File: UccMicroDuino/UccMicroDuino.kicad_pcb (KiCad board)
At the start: 2 copper layers, 45 x 53.5 mm, 14 parts, among them J1 Header, J2 USB_PCB_A, U1 ATtiny85-20S

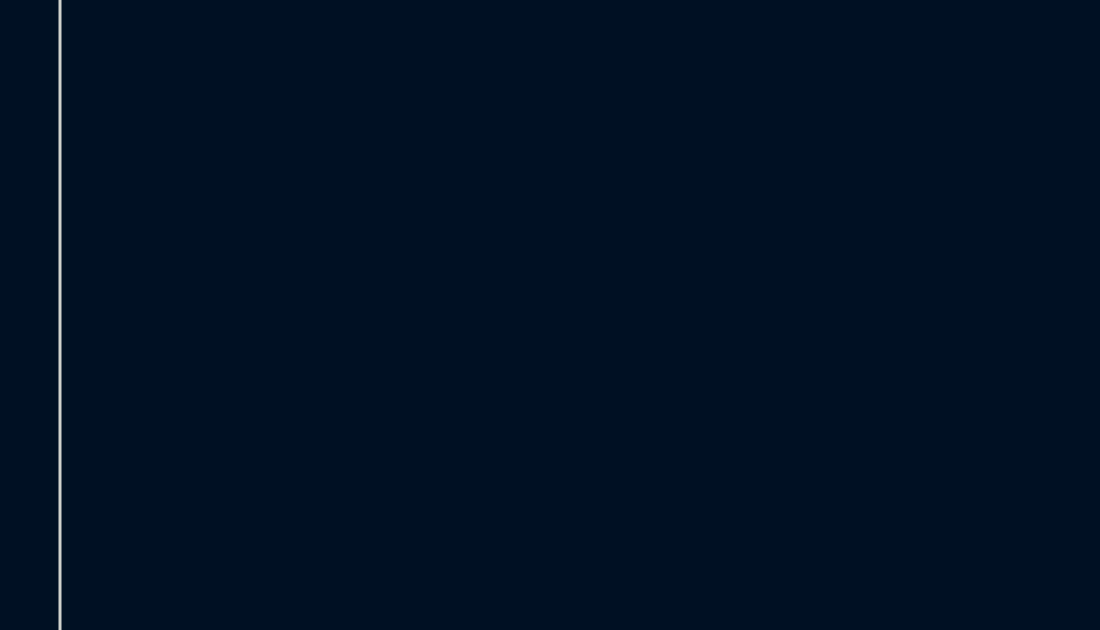
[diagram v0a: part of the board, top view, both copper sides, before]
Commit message: Agrego texto al PCB
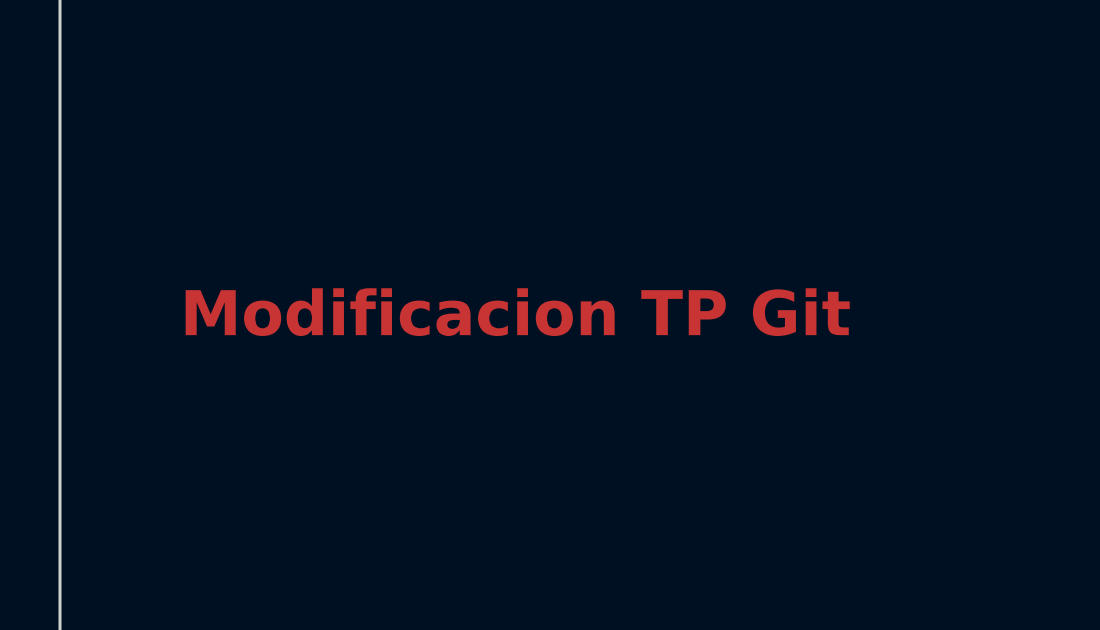
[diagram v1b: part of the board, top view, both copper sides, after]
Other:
- board text added: "Modificacion TP Git"
